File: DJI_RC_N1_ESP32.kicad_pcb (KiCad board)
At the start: 2 copper layers, 57 x 73 mm, 37 parts, among them J4 WE 665102131822, J5 USB_C_Receptacle_USB2.0_16P, U16 USBLC6-2SC6, U2 ESP32-S3-WROOM-1U, U4 MCP73833-xxx-UN

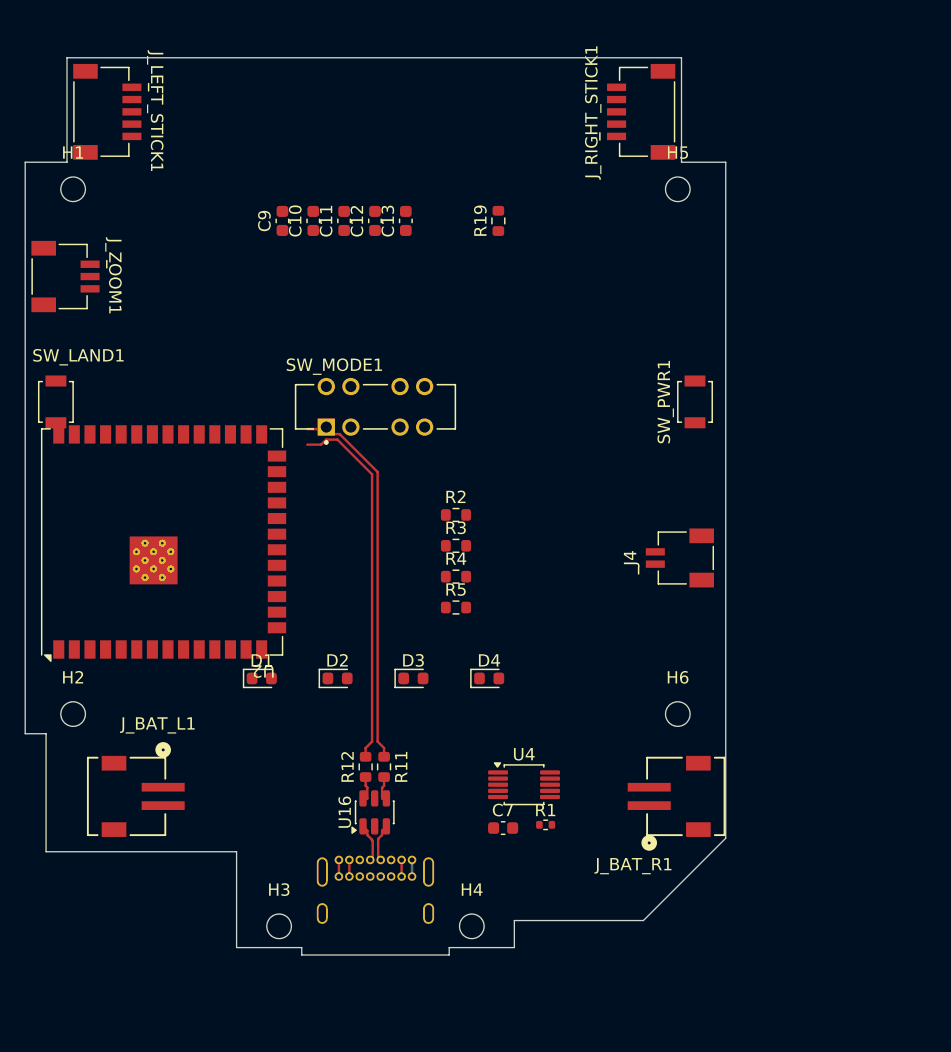
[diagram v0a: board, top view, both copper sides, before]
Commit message: Fix holes positions after 3D print test
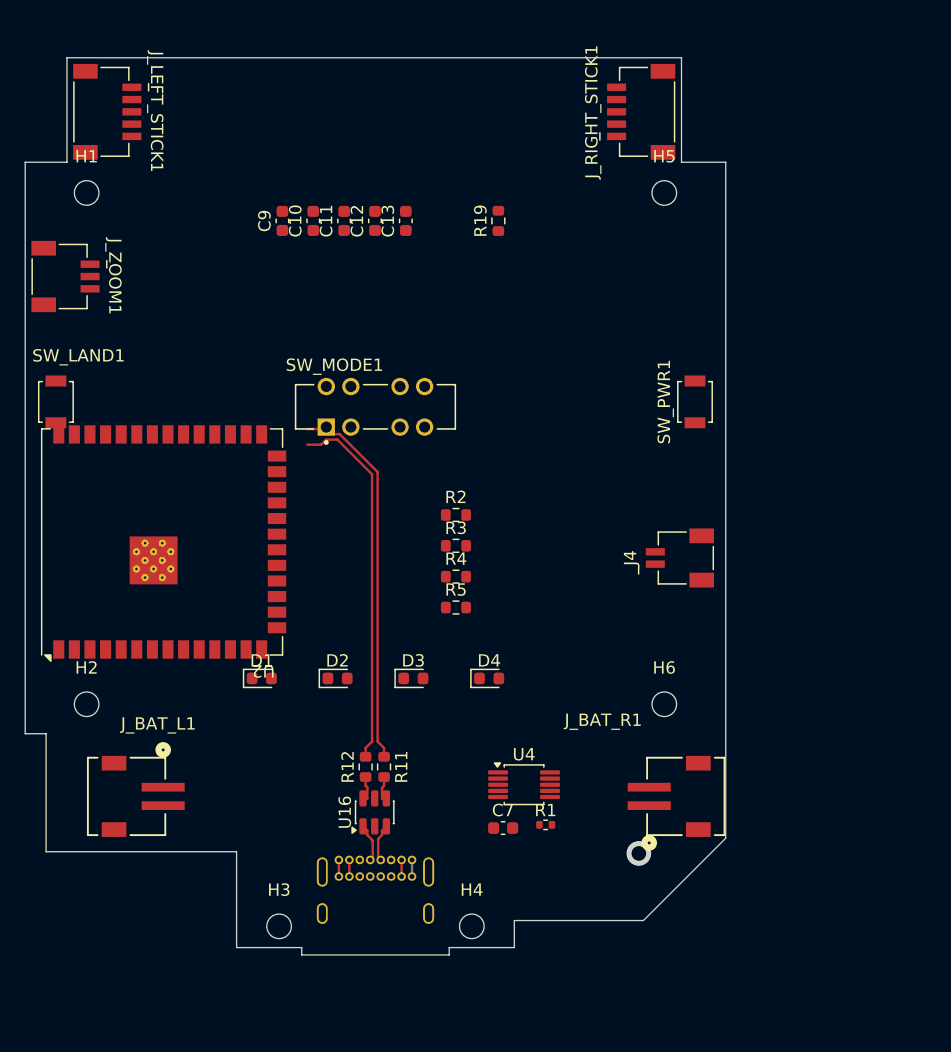
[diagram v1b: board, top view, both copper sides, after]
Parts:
- moved H6 1.36 mm to (52.0, 52.6)
- moved H2 1.36 mm to (5.00, 52.6)
- moved H5 1.14 mm to (52.0, 11.0)
- moved H1 1.14 mm to (5.00, 11.0)
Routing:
- net (no net): vias 0 -> 1
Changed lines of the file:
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@@
 		(locked yes)
 		(layer "F.Cu")
-		(at 53.1 53.4)
+		(at 52 52.6)
 		(descr "Mounting Hole 2mm, no annular, generated by kicad-footprint-generator mountinghole.py")
 		(tags "mountinghole")
@@
 		(model "${USER_3D_MODELS}/665102131822 (rev1).stp"
 			(offset
-				(xyz 0 0 1.5)
+				(xyz 0 0 1.35)
 			)
 			(scale
@@
 		(locked yes)
 		(layer "F.Cu")
-		(at 3.9 53.4)
+		(at 5 52.6)
 		(descr "Mounting Hole 2mm, no annular, generated by kicad-footprint-generator mountinghole.py")
 		(tags "mountinghole")
@@
 		(model "${USER_3D_MODELS}/665105131822 (rev1).stp"
 			(offset
-				(xyz 0 0 1.5)
+				(xyz 0 0 1.35)
 			)
 			(scale
@@
 		(tags "S2B-ZR-SM4A-TFLFSN ")
 		(property "Reference" "J_BAT_R1"
-			(at 5.55 4.2 0)
+			(at -6.2 6.7 0)
 			(unlocked yes)
 			(layer "F.SilkS")
@@
 		(model "${USER_3D_MODELS}/665103131822 (rev1).stp"
 			(offset
-				(xyz 0 0 1.5)
+				(xyz 0 0 1.35)
 			)
 			(scale
@@
 		(locked yes)
 		(layer "F.Cu")
-		(at 53.1 10.7)
+		(at 52 11)
 		(descr "Mounting Hole 2mm, no annular, generated by kicad-footprint-generator mountinghole.py")
 		(tags "mountinghole")
@@
 		(locked yes)
 		(layer "F.Cu")
-		(at 3.9 10.7)
+		(at 5 11)
 		(descr "Mounting Hole 2mm, no annular, generated by kicad-footprint-generator mountinghole.py")
 		(tags "mountinghole")
@@
 		(model "${USER_3D_MODELS}/665105131822 (rev1).stp"
 			(offset
-				(xyz 0 0 1.5)
+				(xyz 0 0 1.35)
 			)
 			(scale
@@
 		(model "${USER_3D_MODELS}/JS203011CQN--3DModel-STEP-510211.step"
 			(offset
-				(xyz 0 0 0)
+				(xyz 0 0 -0.2)
 			)
 			(scale
@@
 		(layer "Edge.Cuts")
 	)
+	(via
+		(at 49.93 64.74)
+		(size 2)
+		(drill 1.2)
+		(layers "F.Cu" "B.Cu")
+		(locked yes)
+		(net "")
+	)
 	(segment

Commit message: ERC pass, Daily save
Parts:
- removed SW_LAND1: SW land, Button_Switch_SMD:SW_SPST_B3U-1000P
- removed SW_PWR1: SW power, Button_Switch_SMD:SW_SPST_B3U-1000P
- added C14: 100nF, Capacitor_SMD:C_0603_1608Metric, F.Cu at (63.6, 68.8)
- added C15: 100nF, Capacitor_SMD:C_0603_1608Metric, F.Cu at (67.2, 35.5)
- added C3: 470pF, Capacitor_SMD:C_0603_1608Metric, F.Cu at (39.4, 37.1)
- added D5: 1N4148WS, Diode_SMD:D_SOD-323, F.Cu at (67.8, 78.0)
- added J_BOOT_TRIGGER1: Conn_01x02_Pin, Connector_PinHeader_2.00mm:PinHeader_1x02_P2.00mm_Vertical, F.Cu at (9.65, 51.9)
- added LS1: Speaker, Buzzer_Beeper:Buzzer_12x9.5RM7.6, F.Cu at (28.5, 54.2)
- added Q1: BSS84, Package_TO_SOT_SMD:SOT-23, F.Cu at (68.1, 69.8)
- added Q2: BSS670S2, Package_TO_SOT_SMD:SOT-23, F.Cu at (68.1, 74.2)
- added Q3: BSS670S2, Package_TO_SOT_SMD:SOT-23, F.Cu at (71.7, 36.5)
- added Q4: BSS670S2, Package_TO_SOT_SMD:SOT-23, F.Cu at (28.6, 36.9)
- added R10: 1K, Resistor_SMD:R_0603_1608Metric, F.Cu at (67.2, 40.5)
- added R13: 100K, Resistor_SMD:R_0603_1608Metric, F.Cu at (67.2, 43.1)
- added R14: 100K, Resistor_SMD:R_0603_1608Metric, F.Cu at (67.2, 45.6)
- added R15: 1K, Resistor_SMD:R_0603_1608Metric, F.Cu at (67.2, 48.1)
- added R16: TBD, Resistor_SMD:R_0603_1608Metric, F.Cu at (27.9, 42.4)
- added R6: 100K, Resistor_SMD:R_0603_1608Metric, F.Cu at (63.6, 71.3)
- added R7: 1K, Resistor_SMD:R_0603_1608Metric, F.Cu at (63.6, 73.8)
- added R8: 100K, Resistor_SMD:R_0603_1608Metric, F.Cu at (63.6, 76.4)
- added R9: 100K, Resistor_SMD:R_0603_1608Metric, F.Cu at (67.2, 38.0)
- added SW1: SW_DPST, footprints:SKRPABE010, F.Cu at (2.50, 28.0)
- added SW2: SW_DPST, footprints:SKRPABE010, F.Cu at (54.5, 28.0)
- added U3: MIC5205-3.3YM5, Package_TO_SOT_SMD:SOT-23-5, F.Cu at (36.9, 37.7)
- moved C10 41.9 mm to (1.80, 49.1), turned to -80 degrees
- moved C9 39.7 mm to (3.30, 48.9), turned to -80 degrees
- moved C11 24.8 mm to (33.0, 37.0), turned to -90 degrees
- moved C12 24.5 mm to (34.5, 37.0), turned to -90 degrees
- moved R2 21.7 mm to (19.2, 52.0)
- moved R3 13.2 mm to (25.4, 48.8)
- moved R11 7.37 mm to (22.5, 54.6)
- moved R12 7.37 mm to (21.0, 54.6)
- moved U16 7.37 mm to (21.8, 58.3)
- moved R4 7.30 mm to (31.6, 48.6)
- moved U4 4.95 mm to (40.8, 64.1)
- moved R5 4.77 mm to (37.7, 48.7)
- moved R1 4.24 mm to (40.8, 66.3)
- moved C7 2.23 mm to (40.8, 61.5)
- moved U2 1.32 mm to (12.4, 39.5), turned to 100 degrees
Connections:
- J4 pad 2: BTN_CAM_CHANGE -> BTN_SHOOT
- J_LEFT_STICK1 pad 2: +3V3 -> +3.3V
- J_RIGHT_STICK1 pad 2: +3V3 -> +3.3V
- J_ZOOM1 pad 2: +3V3 -> +3.3V
- R2 pad 1: LED1_ -> LED_1
- SW_MODE1 pad 1: MODE_SW_CINE_1 -> unconnected-(SW_MODE1-Pad1)
- SW_MODE1 pad 2: MODE_SW_NORMAL_1 -> unconnected-(SW_MODE1-Pad2)
- SW_MODE1 pad 3: MODE_SW_COM_1 -> unconnected-(SW_MODE1-Pad3)
- SW_MODE1 pad 4: MODE_SW_SPORT_1 -> unconnected-(SW_MODE1-Pad4)
- SW_MODE1 pad 7: MODE_SW_COM_2 -> GND
- U2 pad 10: unconnected-(U2-GPIO17/U1TXD/ADC2_CH6-Pad10) -> BUZZER_PWM
- U2 pad 11: unconnected-(U2-GPIO18/U1RXD/ADC2_CH7/CLK_OUT3-Pad11) -> BTN_PWR_MCU
- U2 pad 12: unconnected-(U2-GPIO8/TOUCH8/ADC1_CH7/SUBSPICS1-Pad12) -> AD_VBAT
- U2 pad 15: AN_CH2 -> AD2
- U2 pad 16: BTN0 -> BTN_FN
- U2 pad 17: unconnected-(U2-GPIO9/TOUCH9/ADC1_CH8/FSPIHD/SUBSPIHD-Pad17) -> BTN_SHOOT
- U2 pad 18: LED_0 -> LED_4
- U2 pad 23: BTN1 -> BTN_CAM_CHANGE
- U2 pad 24: BTN2 -> MODE_SW_CINE_2
- U2 pad 25: BTN3 -> MODE_SW_NORMAL_2
- U2 pad 26: unconnected-(U2-GPIO45-Pad26) -> MODE_SW_SPORT_2
- U2 pad 31: unconnected-(U2-GPIO38/FSPIWP/SUBSPIWP-Pad31) -> KEEP_PWR
- U2 pad 38: AN_CH1 -> AD1
- U2 pad 39: AN_CH0 -> AD_ZOOM
- U2 pad 4: AN_CH3 -> AD3
- U2 pad 5: unconnected-(U2-GPIO5/TOUCH5/ADC1_CH4-Pad5) -> AD0
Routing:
- net GND: track 2.70 -> 96.5 mm, vias 0 -> 10
- net VBAT: track 0.00 -> 51.4 mm, vias 0 -> 4
- net /ESP/USB_D_R_P: track 30.6 -> 7.68 mm
- net /ESP/USB_D_R_N: track 29.8 -> 7.37 mm
- net Net-(U16-VBUS): track 2.70 -> 20.1 mm
- net MODE_SW_SPORT_2: track 0.00 -> 17.1 mm
- net AD_ZOOM: track 0.00 -> 13.9 mm
- net MODE_SW_NORMAL_2: track 0.00 -> 11.5 mm
- net +3.3V: track 0.00 -> 9.47 mm
- net MODE_SW_CINE_2: track 0.00 -> 8.74 mm
- net /Charger/USB_UNPROT_DP: track 3.09 -> 11.2 mm
- net /Charger/USB_UNPROT_DN: track 3.15 -> 11.2 mm
- net Net-(J_BOOT_TRIGGER1-Pin_1): track 0.00 -> 3.27 mm
- net Net-(U4-PROG): track 0.00 -> 2.59 mm
- net BOOT/BTN_LAND: track 0.00 -> 2.15 mm
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- added copper zone on B.Cu, net GND
- added copper zone on F.Cu, net GND

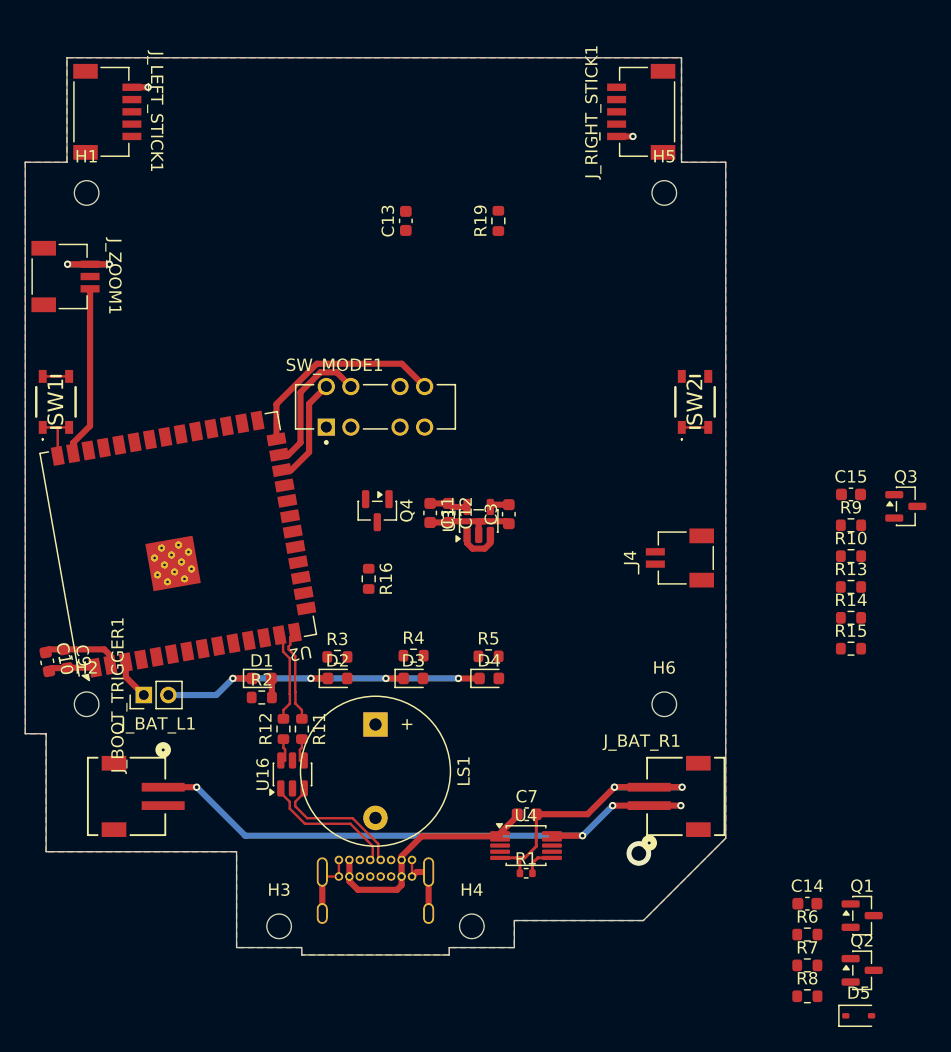
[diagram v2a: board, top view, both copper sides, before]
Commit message: Board had been routedy
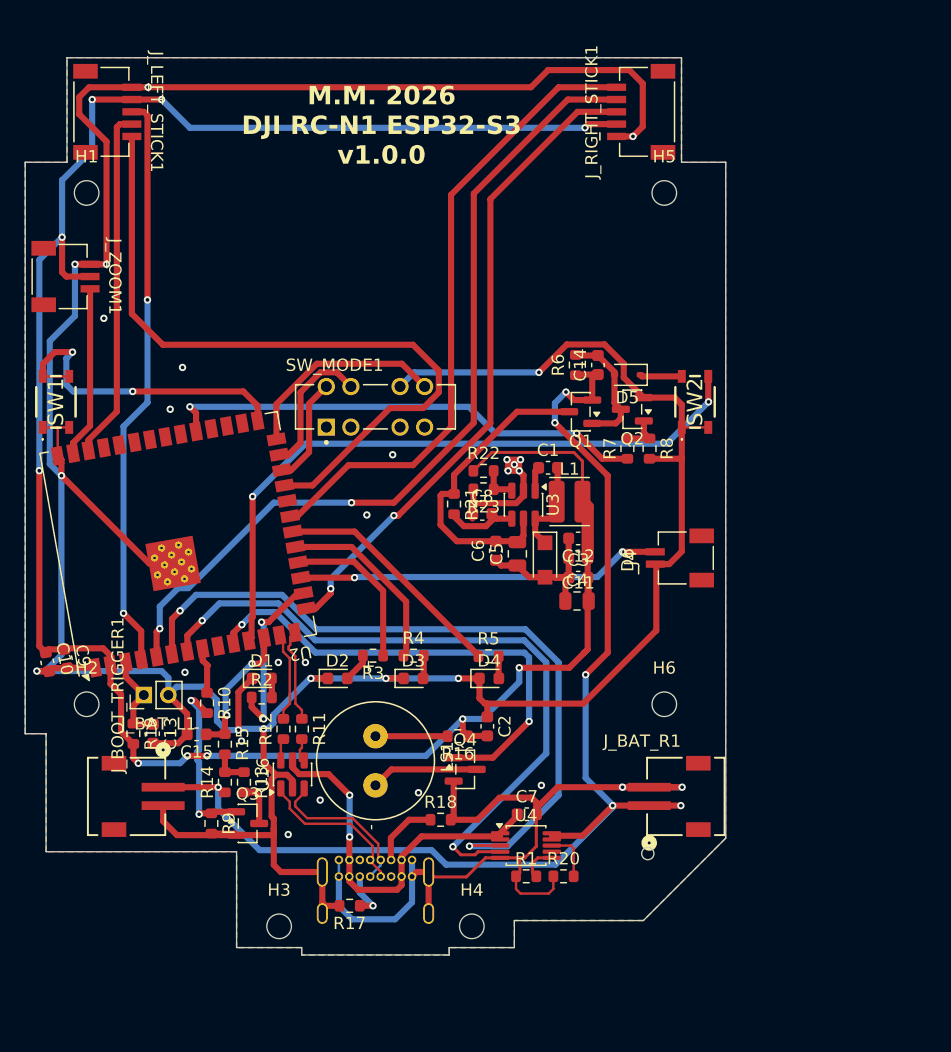
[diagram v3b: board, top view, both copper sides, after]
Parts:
- added C1: 100nF, Capacitor_SMD:C_0603_1608Metric, F.Cu at (42.5, 33.4)
- added C2: 100nF, Capacitor_SMD:C_0603_1608Metric, F.Cu at (37.6, 54.4)
- added C4: 10uF, Capacitor_SMD:C_0805_2012Metric, F.Cu at (44.9, 44.2)
- added C5: 2u2, Capacitor_SMD:C_0805_2012Metric, F.Cu at (40.0, 40.4)
- added C6: 100nF, Capacitor_SMD:C_0603_1608Metric, F.Cu at (38.3, 40.1)
- added C8: 100nF, Capacitor_SMD:C_0603_1608Metric, F.Cu at (37.2, 37.1)
- added D6: PMEG10010ELR, Diode_SMD:Nexperia_CFP3_SOD-123W, F.Cu at (42.3, 40.9)
- added L1: 74404032220, Inductor_SMD:L_Wuerth_MAPI-3015, F.Cu at (44.3, 36.1)
- added R17: 5K1, Resistor_SMD:R_0603_1608Metric, F.Cu at (26.4, 69.0)
- added R18: 5K1, Resistor_SMD:R_0603_1608Metric, F.Cu at (33.8, 62.0)
- added R20: 10K, Resistor_SMD:R_0603_1608Metric, F.Cu at (43.8, 66.6)
- added R21: TBD, Resistor_SMD:R_0603_1608Metric, F.Cu at (34.9, 36.3)
- added R22: 33K, Resistor_SMD:R_0603_1608Metric, F.Cu at (37.3, 33.6)
- added R23: 10K, Resistor_SMD:R_0603_1608Metric, F.Cu at (37.3, 35.1)
- C3: value 470pF -> 10uF
- LS1: footprint Buzzer_Beeper:Buzzer_12x9.5RM7.6 -> footprints:XDCR_CMT-9605-85T
- R1: footprint Resistor_SMD:R_0402_1005Metric -> Resistor_SMD:R_0603_1608Metric
- U3: value MIC5205-3.3YM5 -> LV2862XDDC; footprint Package_TO_SOT_SMD:SOT-23-5 -> Package_TO_SOT_SMD:SOT-23-6
- moved Q3 59.4 mm to (18.1, 62.3)
- moved R9 57.4 mm to (15.2, 62.3), turned to -90 degrees
- moved C15 56.7 mm to (13.9, 55.0), turned to 180 degrees
- moved D5 55.4 mm to (49.0, 25.8), turned to 180 degrees
- moved R10 53.7 mm to (14.8, 52.5), turned to -90 degrees
- moved R14 52.7 mm to (16.2, 59.0), turned to 90 degrees
- moved R13 51.9 mm to (17.8, 59.0), turned to -90 degrees
- moved R15 51.5 mm to (16.2, 55.9), turned to -90 degrees
- moved R19 51.2 mm to (8.80, 55.0), turned to -90 degrees
- moved R6 50.0 mm to (44.8, 25.0), turned to 90 degrees
- moved Q2 49.3 mm to (49.4, 28.6), turned to 180 degrees
- moved C14 47.0 mm to (46.6, 25.0), turned to 90 degrees
- moved Q1 47.0 mm to (45.2, 28.8), turned to 180 degrees
- moved C13 46.5 mm to (10.4, 55.0), turned to -90 degrees
- moved R8 46.4 mm to (50.8, 31.8), turned to -90 degrees
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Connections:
- net /Charger/USB_UNPROT_DN renamed /Charger and +3V3 DCDC/USB_UNPROT_DN
- net /Charger/USB_UNPROT_DP renamed /Charger and +3V3 DCDC/USB_UNPROT_DP
- C3 pad 2: Net-(U3-BP) -> +3.3V
- J5 pad A5: unconnected-(J5-CC1-PadA5) -> Net-(J5-CC1)
- J5 pad B5: unconnected-(J5-CC2-PadB5) -> Net-(J5-CC2)
- U2 pad 16: BTN_FN -> LED_1
- U2 pad 18: LED_4 -> LED_2
- U2 pad 20: LED_2 -> LED_4
- U2 pad 21: LED_1 -> BTN_CAM_CHANGE
- U2 pad 23: BTN_CAM_CHANGE -> BTN_FN
- U2 pad 4: AD3 -> AD0
- U2 pad 5: AD0 -> AD3
- U2 pad 8: unconnected-(U2-GPIO15/U0RTS/ADC2_CH4/XTAL_32K_P-Pad8) -> MEASURE_VBAT_EN
- U3 pad 1: VBAT -> Net-(U3-CB)
- U3 pad 3: VBAT -> Net-(U3-FB)
- U3 pad 4: Net-(U3-BP) -> Net-(U3-~{SHDN})
- U3 pad 5: +3.3V -> VBAT_SWITCHED
- U4 pad 8: unconnected-(U4-THERM-Pad8) -> Net-(U4-THERM)
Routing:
- net GND: track 96.5 -> 392.6 mm, vias 10 -> 32
- net +3.3V: track 9.47 -> 183.1 mm, vias 0 -> 10
- net AD3: track 0.00 -> 69.4 mm, vias 0 -> 2
- net CHARGER_ST1: track 0.00 -> 59.7 mm, vias 0 -> 2
- net BTN_FN: track 0.00 -> 59.3 mm
- net CHARGER_ST2: track 0.00 -> 55.9 mm, vias 0 -> 2
- net BTN_PWR_MCU: track 0.00 -> 54.2 mm, vias 0 -> 2
- net AD2: track 0.00 -> 53.4 mm, vias 0 -> 2
- net BTN_CAM_CHANGE: track 0.00 -> 52.1 mm
- net VBAT: track 51.4 -> 98.9 mm, vias 4 -> 6
- net AD0: track 0.00 -> 47.1 mm, vias 0 -> 2
- net BUZZER_PWM: track 0.00 -> 39.7 mm, vias 0 -> 2
- net KEEP_PWR: track 0.00 -> 39.6 mm, vias 0 -> 2
- net BTN_SHOOT: track 0.00 -> 29.7 mm, vias 0 -> 2
- net AD1: track 0.00 -> 28.6 mm
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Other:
- outline, holes or cut-outs redrawn
- copper layers 2 -> 4
- board text added: "M.M. 2026 DJI RC-N1 ESP32-S3 v1.0.0"

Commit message: Daily save
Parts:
- added J2: Conn_01x03, Connector_PinHeader_2.54mm:PinHeader_1x03_P2.54mm_Vertical, F.Cu at (8.96, 25.6)
- moved C3 43.2 mm to (2.00, 46.2), turned to -170 degrees
- moved C11 15.6 mm to (37.6, 54.4), turned to 90 degrees
- moved C2 13.7 mm to (45.1, 42.9), turned to 0 degrees
- moved C4 4.91 mm to (45.2, 39.3)
- moved C12 2.19 mm to (45.0, 41.3)
- moved SW_MODE1 0.70 mm to (28.5, 29.1)
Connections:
- U2 pad 36: unconnected-(U2-U0RXD/GPIO44/CLK_OUT2-Pad36) -> /ESP/U0RX
- U2 pad 37: unconnected-(U2-U0TXD/GPIO43/CLK_OUT1-Pad37) -> /ESP/U0TX
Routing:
- net /ESP/U0RX: track 0.00 -> 8.21 mm, vias 0 -> 1
- net /ESP/U0TX: track 0.00 -> 7.19 mm
- net BOOT/BTN_LAND: track 26.3 -> 21.8 mm
- net AD_ZOOM: track 13.9 -> 15.3 mm
- net GND: track 392.6 -> 391.5 mm, vias 32 -> 31
- net MODE_SW_CINE_2: track 8.74 -> 8.04 mm
- net AD0: track 47.1 -> 47.7 mm
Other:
- copper layers 4 -> 2
- board text added: "GND"
- board text added: "U0RX"
- board text added: "U0TX"
